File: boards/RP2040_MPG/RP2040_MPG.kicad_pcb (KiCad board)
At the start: 2 copper layers, 3 parts, among them U2 RS485_2_TTL_UART

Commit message: WIP
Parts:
- added H1: MountingHole, MountingHole:MountingHole_3.2mm_M3_DIN965, F.Cu at (22.9, 139.7)
- added H2: MountingHole, MountingHole:MountingHole_3.2mm_M3_DIN965, F.Cu at (22.9, 175.3)
- added H3: MountingHole, MountingHole:MountingHole_3.2mm_M3_DIN965, F.Cu at (78.7, 139.7)
- added H4: MountingHole, MountingHole:MountingHole_3.2mm_M3_DIN965, F.Cu at (78.7, 176.5)
- added J1: RJ12, Connector_RJ:RJ12_Amphenol_54601, B.Cu at (66.0, 160.0)
- added J2: Conn_01x04_Socket, Connector_Molex:Molex_KK-254_AE-6410-04A_1x04_P2.54mm_Vertical, B.Cu at (74.9, 171.4)
- added SW1: SW_Push, Heli2:Drucktaster_12x12, F.Cu at (30.5, 154.9)
- added SW2: SW_Push, Heli2:Drucktaster_12x12, F.Cu at (43.2, 154.9)
- added SW3: SW_Push, Heli2:Drucktaster_12x12, F.Cu at (55.9, 154.9)
- added SW4: SW_Push, Heli2:Drucktaster_12x12, F.Cu at (68.6, 154.9)
- RZ1, U2: moved to B.Cu
- moved RZ1 69.5 mm to (52.4, 158.6), turned to -90 degrees
- moved Brd1 62.7 mm to (49.5, 127.0), turned to 180 degrees
- moved U2 33.8 mm to (73.7, 141.1), turned to 180 degrees
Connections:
- Brd1 pad 1: GND -> Net-(Brd1-VCC)
- Brd1 pad 2: Net-(Brd1-VCC) -> GND
- RZ1 pad 11: unconnected-(RZ1-GP10-Pad11) -> Net-(J2-Pin_4)
- RZ1 pad 12: unconnected-(RZ1-GP11-Pad12) -> Net-(J2-Pin_3)
- RZ1 pad 14: unconnected-(RZ1-GP13-Pad14) -> Net-(RZ1-GP13)
- RZ1 pad 15: unconnected-(RZ1-GP14-Pad15) -> Net-(RZ1-GP14)
- RZ1 pad 16: unconnected-(RZ1-GP15-Pad16) -> Net-(RZ1-GP15)
- RZ1 pad 22: unconnected-(RZ1-5V-Pad22) -> Net-(RZ1-5V)
- U2 pad 7: Net-(U2-Y) -> GND
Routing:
- net GND: track 0.00 -> 119.0 mm
- net Net-(Brd1-VCC): track 0.00 -> 79.2 mm
- net Net-(Brd1-SDA): track 0.00 -> 45.5 mm
- net Net-(RZ1-5V): track 0.00 -> 40.1 mm
- net Net-(Brd1-SCL): track 0.00 -> 38.2 mm
- net Net-(RZ1-GP1): track 0.00 -> 31.1 mm
- net Net-(J2-Pin_4): track 0.00 -> 30.6 mm
- net Net-(RZ1-GP0): track 0.00 -> 28.2 mm
- net Net-(J2-Pin_3): track 0.00 -> 24.4 mm
- net Net-(RZ1-GP13): track 0.00 -> 20.7 mm
- net Net-(U2-B-): track 0.00 -> 18.6 mm
- net Net-(RZ1-GP26): track 0.00 -> 17.3 mm
- net Net-(U2-A+): track 0.00 -> 13.8 mm
- net Net-(RZ1-GP14): track 0.00 -> 7.18 mm
- net Net-(RZ1-GP15): track 0.00 -> 7.18 mm
- added copper zone on B.Cu, net GND
- added copper zone on F.Cu, net GND
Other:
- board outline added: 63.5 x 44.5 mm
- board text added: "MPG Wheel with DRO"

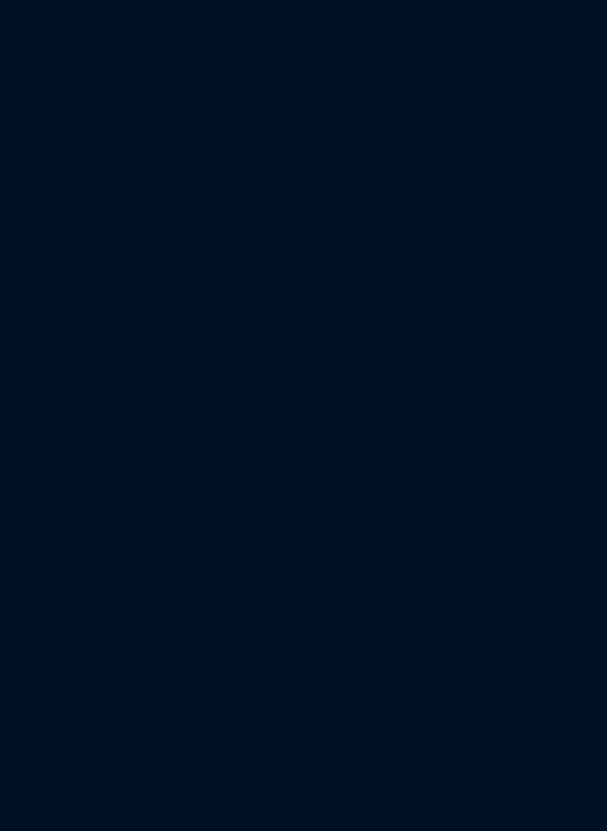
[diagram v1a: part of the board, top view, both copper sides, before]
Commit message: change rc filter
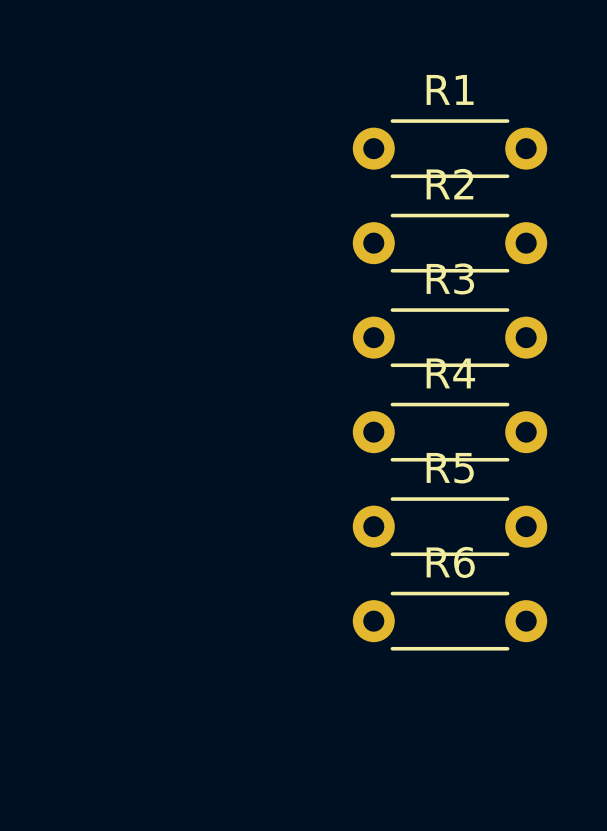
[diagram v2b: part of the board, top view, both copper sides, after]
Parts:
- added R1: 4k7, Resistor_THT:R_Axial_DIN0204_L3.6mm_D1.6mm_P5.08mm_Horizontal, F.Cu at (89.2, 105.7)
- added R2: 4k7, Resistor_THT:R_Axial_DIN0204_L3.6mm_D1.6mm_P5.08mm_Horizontal, F.Cu at (89.2, 108.8)
- added R3: 4k7, Resistor_THT:R_Axial_DIN0204_L3.6mm_D1.6mm_P5.08mm_Horizontal, F.Cu at (89.2, 112.0)
- added R4: 4k7, Resistor_THT:R_Axial_DIN0204_L3.6mm_D1.6mm_P5.08mm_Horizontal, F.Cu at (89.2, 115.1)
- added R5: 4k7, Resistor_THT:R_Axial_DIN0204_L3.6mm_D1.6mm_P5.08mm_Horizontal, F.Cu at (89.2, 118.3)
- added R6: 4k7, Resistor_THT:R_Axial_DIN0204_L3.6mm_D1.6mm_P5.08mm_Horizontal, F.Cu at (89.2, 121.4)
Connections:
- J1 pad 1: Net-(RZ1-5V) -> Net-(J2-Pin_1)
- J2 pad 1: Net-(Brd1-VCC) -> Net-(J2-Pin_1)
- RZ1 pad 11: Net-(J2-Pin_4) -> Net-(RZ1-GP10)
- RZ1 pad 12: Net-(J2-Pin_3) -> Net-(RZ1-GP11)
- RZ1 pad 22: Net-(RZ1-5V) -> Net-(J2-Pin_1)
- SW1 pad 1: Net-(RZ1-GP26) -> Net-(C6-Pad2)
- SW2 pad 1: Net-(RZ1-GP15) -> Net-(C5-Pad1)
- SW3 pad 1: Net-(RZ1-GP14) -> Net-(C4-Pad1)
- SW4 pad 1: Net-(RZ1-GP13) -> Net-(C3-Pad1)
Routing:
- net Net-(RZ1-5V): track 40.1 -> 0.00 mm
- net Net-(J2-Pin_1): track 0.00 -> 40.1 mm
